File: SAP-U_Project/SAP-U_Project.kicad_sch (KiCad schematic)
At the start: 0 parts

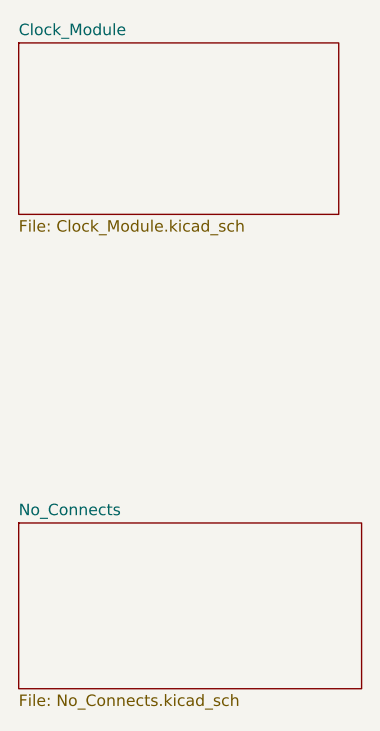
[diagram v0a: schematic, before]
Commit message: Checkpoint: removed simulation, cleaned up schematic
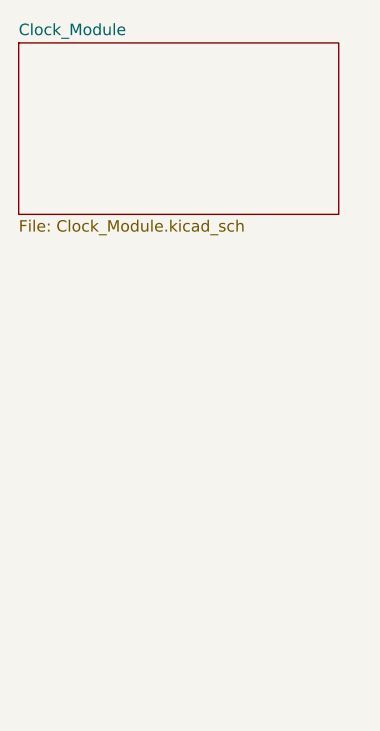
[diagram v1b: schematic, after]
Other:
- removed sheet No_Connects
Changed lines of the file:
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@@
-		)
-	)
-	(sheet
-		(at 30.48 82.55)
-		(size 38.1 18.415)
-		(fields_autoplaced yes)
-		(stroke
-			(width 0.1524)
-			(type solid)
-		)
-		(fill
-			(color 0 0 0 0.0000)
-		)
-		(property "Sheetname" "No_Connects"
-			(at 30.48 81.8384 0)
-			(effects
-				(font
-					(size 1.27 1.27)
-				)
-				(justify left bottom)
-			)
-		)
-		(property "Sheetfile" "No_Connects.kicad_sch"
-			(at 30.48 101.5496 0)
-			(effects
-				(font
-					(size 1.27 1.27)
-				)
-				(justify left top)
-			)
-		)
-		(instances
-			(project "SAP-U_Project"
-				(path "/e63e39d7-6ac0-4ffd-8aa3-1841a4541b55"
-					(page "0")
-				)
-			)
 		)
 	)

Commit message: Checkpoint: completed schematic for Clock Module
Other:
- added sheet No_Connects (No_Connects.kicad_sch)
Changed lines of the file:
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@@
+		)
+	)
+	(sheet
+		(at 30.48 82.55)
+		(size 38.1 18.415)
+		(fields_autoplaced yes)
+		(stroke
+			(width 0.1524)
+			(type solid)
+		)
+		(fill
+			(color 0 0 0 0.0000)
+		)
+		(property "Sheetname" "No_Connects"
+			(at 30.48 81.8384 0)
+			(effects
+				(font
+					(size 1.27 1.27)
+				)
+				(justify left bottom)
+			)
+		)
+		(property "Sheetfile" "No_Connects.kicad_sch"
+			(at 30.48 101.5496 0)
+			(effects
+				(font
+					(size 1.27 1.27)
+				)
+				(justify left top)
+			)
+		)
+		(instances
+			(project "SAP-U_Project"
+				(path "/e63e39d7-6ac0-4ffd-8aa3-1841a4541b55"
+					(page "3")
+				)
+			)
 		)
 	)
